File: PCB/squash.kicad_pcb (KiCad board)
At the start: 2 copper layers, 247.7 x 101.6 mm, 75 parts, among them J1 SSD1306, J2 Conn_01x05, J3 Conn_01x02, J4 Conn_01x02, SW1 1.50u, SW10 1.00u, SW11 1.00u, SW12 1.50u, SW13 1.75u_stepped_caps_lock, SW14 1.00u, SW15 1.00u, SW16 1.00u, SW17 1.00u, SW18 1.00u, SW19 1.00u, SW2 1.00u, SW20 1.00u, SW21 1.00u, SW22 1.00u, SW23 2.25u, SW24 1.00u, SW25 1.00u, SW26 1.00u, SW27 1.00u, SW28 1.00u, SW29 1.00u, SW3 1.00u, SW30 1.00u, SW31 1.00u, SW32 1.00u, SW33 1.75u, SW34 2.25u_or_1.25and1.00, SW35 1.25u, SW36 1.00u, SW37 1.00u, SW38 6.25u, SW39 1.25u, SW4 1.00u, SW40 1.00u, SW41 1.25u, SW42 1.25u, SW43 2.25u, SW44 1.00u, SW45 2.75u, SW5 1.00u, SW6 1.00u, SW7 1.00u, SW8 1.00u, SW9 1.00u, U1 STM32F072V8Tx, U2 AMS1117-3.3

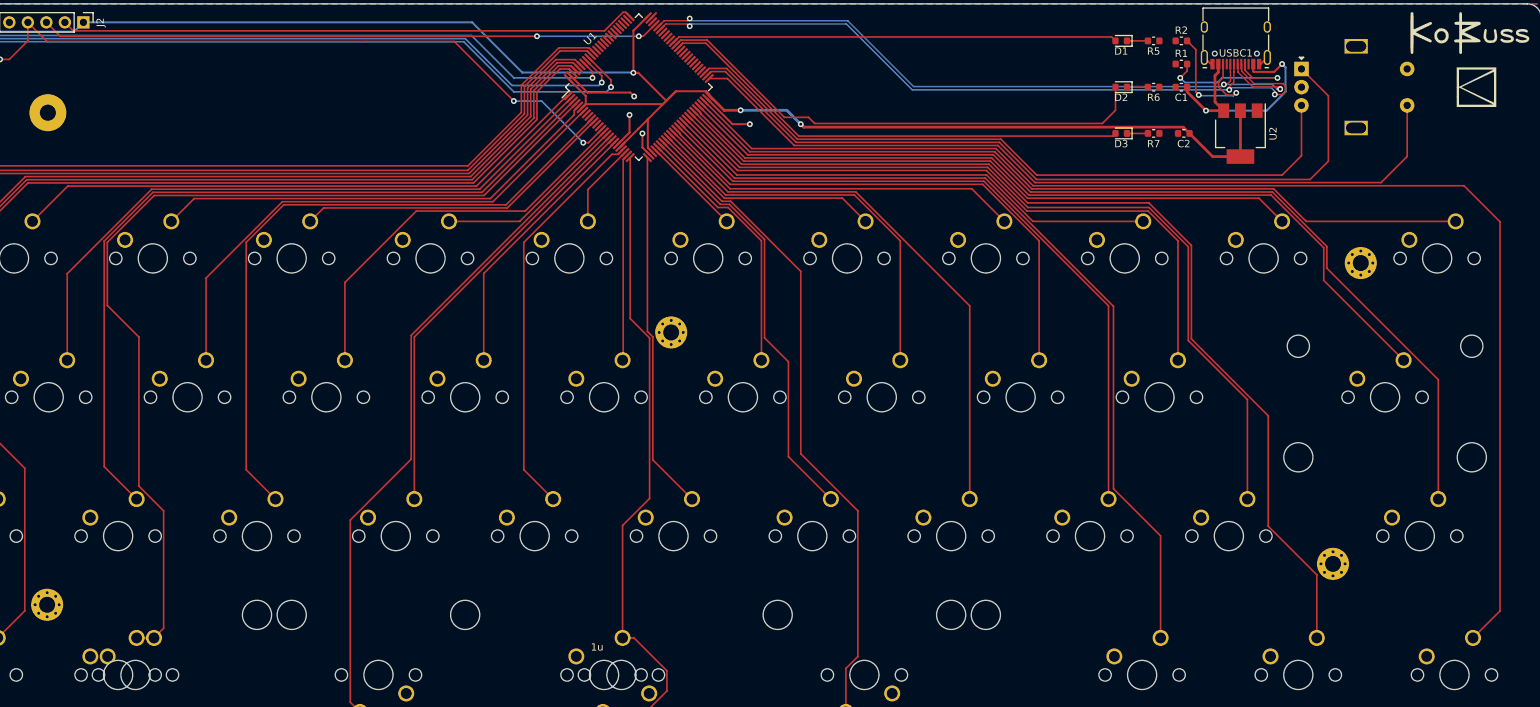
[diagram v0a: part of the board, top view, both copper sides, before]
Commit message: Left alt key pcb label, removal of logo
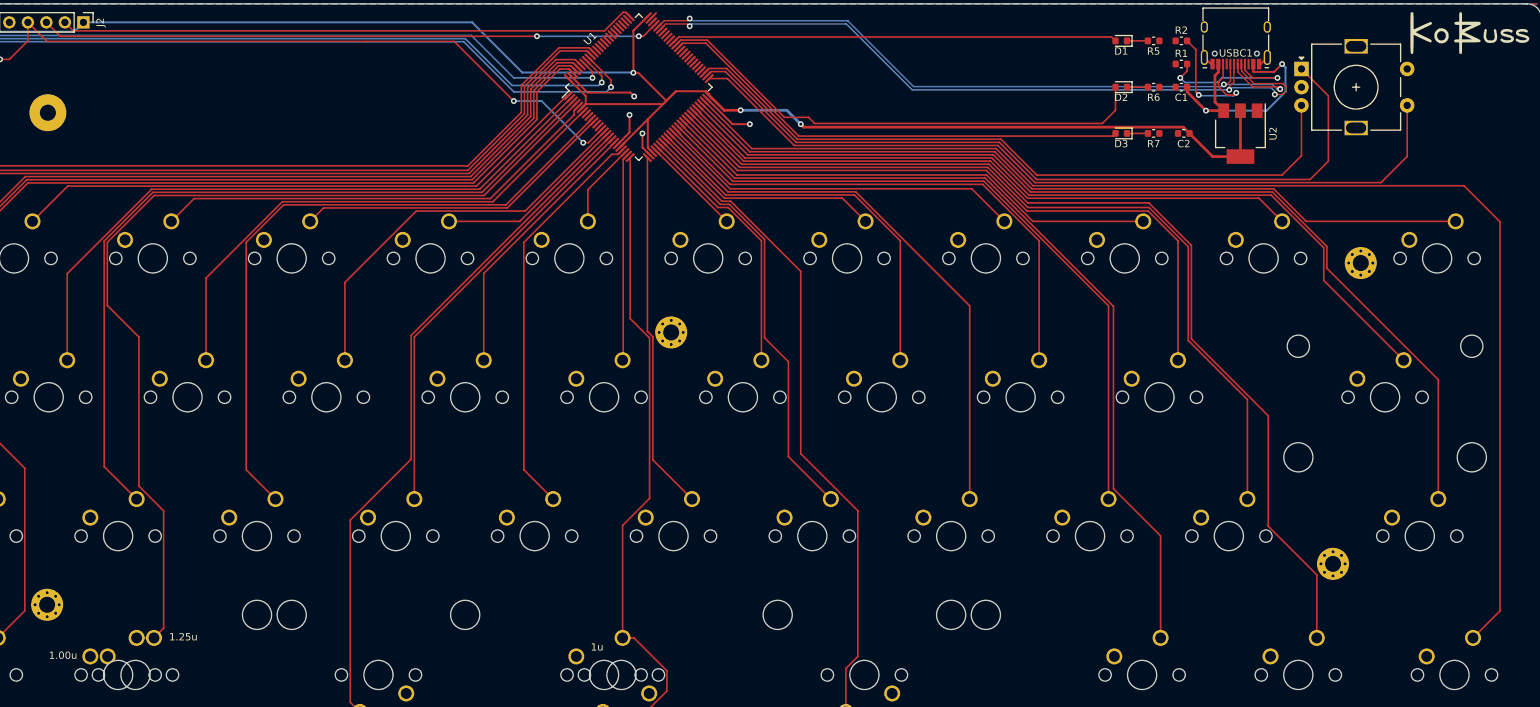
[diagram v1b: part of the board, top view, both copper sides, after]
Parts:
- removed the Ref** at (238.8, 12.7)
- removed the Ref** at (238.8, 11.4)
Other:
- board text added: "1.00u"
- board text added: "1.25u"
